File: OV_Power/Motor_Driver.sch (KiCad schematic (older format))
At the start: 15 parts, among them CN1 CONN_HEADER_R_A_2POS_2.5MM, U3 LT6106, U4 VNH5019ATR-E

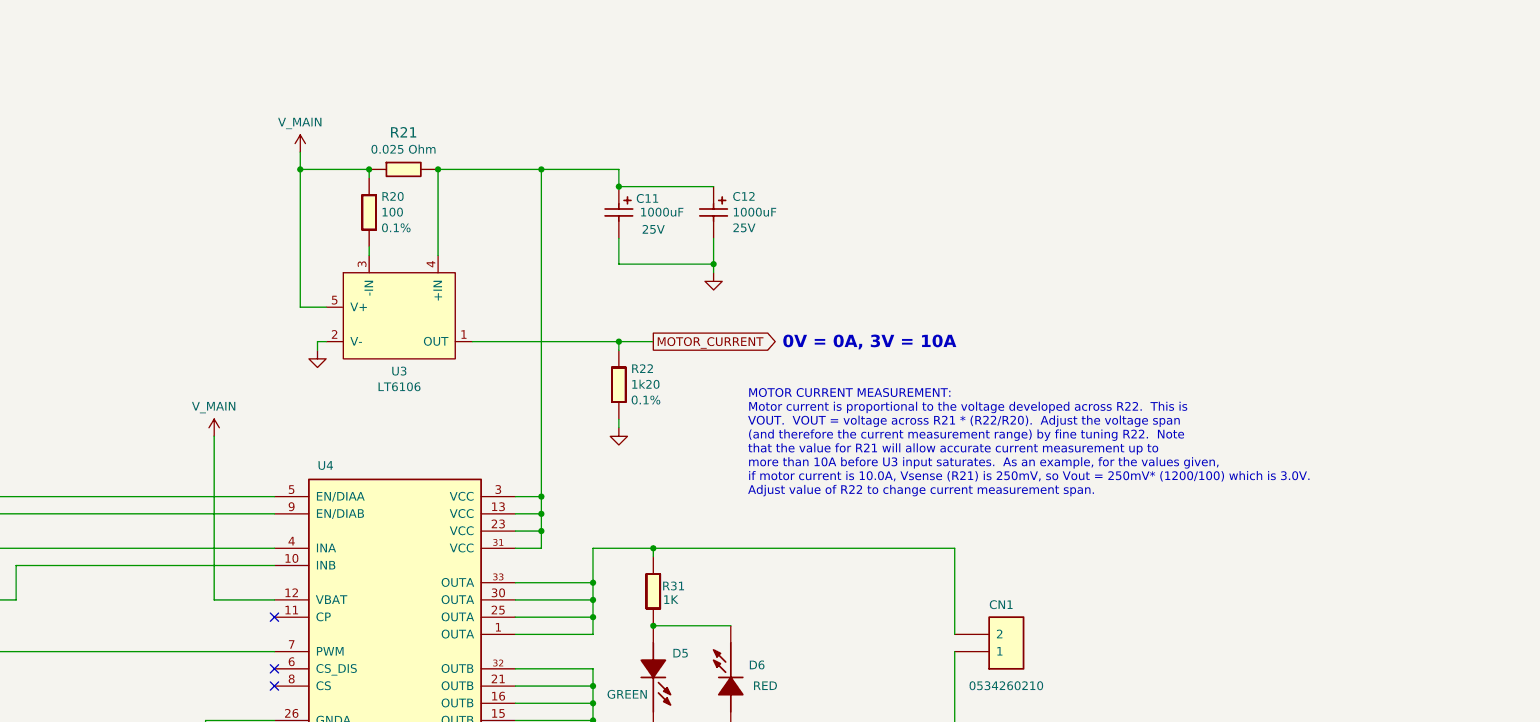
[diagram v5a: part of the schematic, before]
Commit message: First cut at complete routing for the power board.  Still need DRC checking and final fettling of the BOM and silkscreens before going to press.
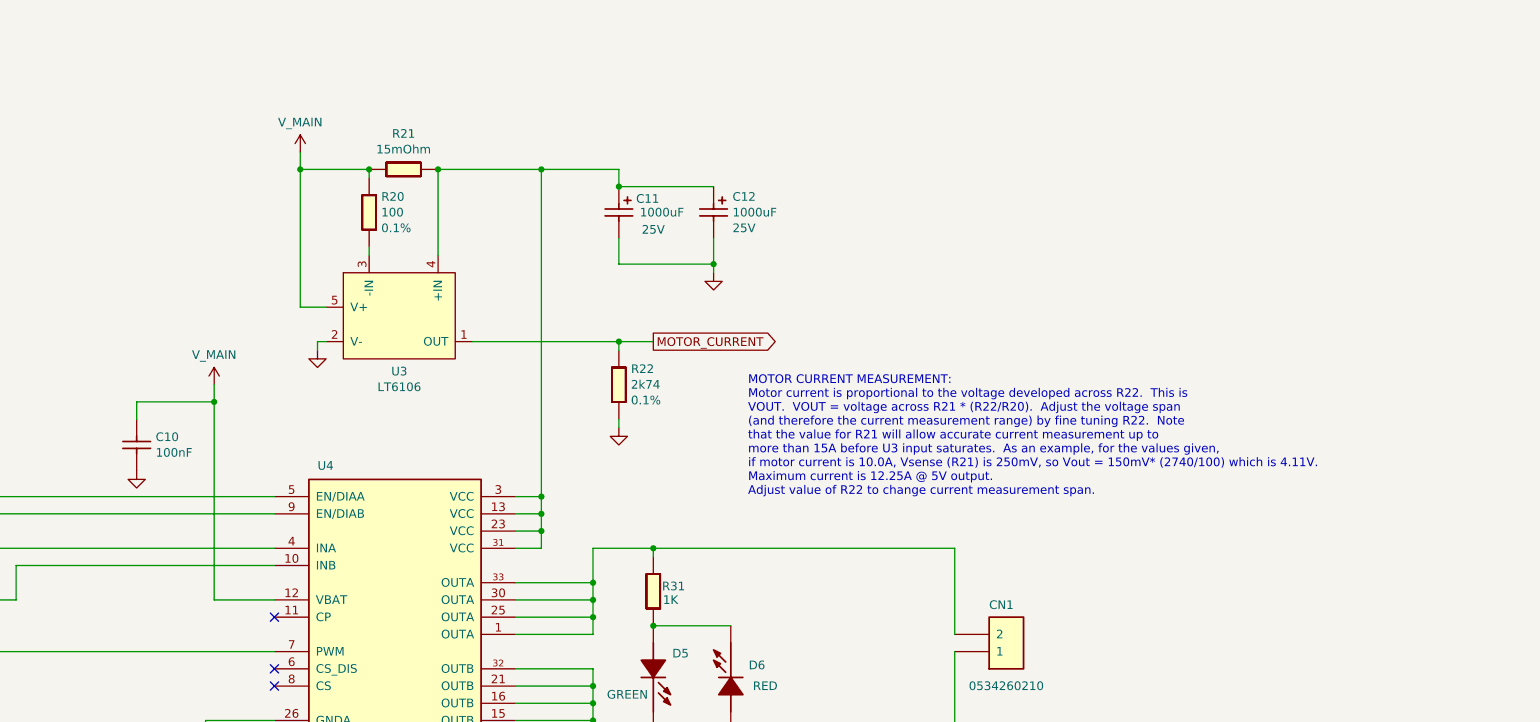
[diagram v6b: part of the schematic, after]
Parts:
- removed R21: 0.025 Ohm, Resistor_SMD:R_2010_5025Metric, symbol OpenVent:Resistor_2010_0.025OHM_sensing_1%_1W
- removed R22: R_0603_1k2_0.1W_0.1%, Resistor_SMD:R_0603_1608Metric, symbol OpenVent:R_0603_1k2_0.1W_0.1%
- added C10: 100nF_0603_Ceramic_Capacitor,_10%,_X7R,_25V, Capacitor_SMD:C_0603_1608Metric, symbol OpenVent:100nF_0603_Ceramic_Capacitor,_10%,_X7R,_25V
- added R21: R_2512_15m_cursense, Resistor_SMD:R_2512_6332Metric, symbol OpenVent:R_2512_15m_cursense
- added R22: R_0603_2k74_0.1W_0.1%, Resistor_SMD:R_0603_1608Metric, symbol OpenVent:R_0603_2k74_0.1W_0.1%
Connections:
- net GND: now also C10.2, R22.2
- net MOTOR_CURRENT: now also R22.1
- net V_MAIN: now also C10.1, R21.1
- net at C11.1 (+), C12.1 (+), U3.4 (+IN)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: now also R21.2
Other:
- note added: "MOTOR CURRENT MEASUREMENT:\nMotor current is proportional to the voltage developed across R22. This is\nVOUT. VOUT = voltage across R21 * (R22/R20). Adjust the voltage span\n(and therefore the current measurement range) by fine tuning R22. Note\nthat the value for R21 will allow accurate current measurement up to\nmore than 15A before U3 input saturates. As an example, for the values given,\nif m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"
- note removed: "0V = 0A, 3V = 10A"
- note removed: "MOTOR CURRENT MEASUREMENT:\nMotor current is proportional to the voltage developed across R22. This is\nVOUT. VOUT = voltage across R21 * (R22/R20). Adjust the voltage span\n(and therefore the current measurement range) by fine tuning R22. Note\nthat the value for R21 will allow accurate current measurement up to\nmore than 10A before U3 input saturates. As an example, for the values given,\nif m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"
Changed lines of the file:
@@
 	4200 3650 4550 3650
 Wire Wire Line
-	4200 2700 4200 3650
+	4200 2400 4200 2500
 Wire Wire Line
 	6400 4500 6400 4350
@@
 L OpenVent:V_MAIN #PWR019
 U 1 1 5FC35966
-P 4200 2700
-F 0 "#PWR019" H 4200 2550 50  0001 C CNN
-F 1 "V_MAIN" H 4200 2873 50  0000 C CNN
-F 2 "" H 4200 2700 50  0001 C CNN
-F 3 "" H 4200 2700 50  0001 C CNN
-	1    4200 2700
+P 4200 2400
+F 0 "#PWR019" H 4200 2250 50  0001 C CNN
+F 1 "V_MAIN" H 4200 2573 50  0000 C CNN
+F 2 "" H 4200 2400 50  0001 C CNN
+F 3 "" H 4200 2400 50  0001 C CNN
+	1    4200 2400
 	1    0    0    -1
 $EndComp
@@
 Connection ~ 6550 2150
 Text Notes 7300 3050 0    50   ~ 0
-MOTOR CURRENT MEASUREMENT:\nMotor current is proportional to the voltage developed across R22.  This is\nVOUT.  VOUT = voltage across R21 * (R22/R20).  Adjust the voltage span\n(and therefore the current measurement range) by fine tuning R22.  Note\nthat the value for R21 will allow accurate current measurement up to\nmore than 10A before U3 input saturates.  As an example, for the values given,\nif motor current is 10.0A, Vsense (R21) is 250mV, so Vout = 250mV* (1200/100) which is 3.0V.\nAdjust value of R22 to change current measurement span.
-$Comp
-L OpenVent:Resistor_2010_0.025OHM_sensing_1%_1W R21
-U 1 1 5FD70E6B
-P 5200 1050
-F 0 "R21" H 5300 1163 60  0000 C CNN
-F 1 "0.025 Ohm" H 5300 1065 50  0000 C CNN
-F 2 "Resistor_SMD:R_2010_5025Metric" H 5200 750 60  0001 C CNN
-F 3 "" H 5200 1050 60  0001 C CNN
-F 4 "Vishay Dale" H 5900 1000 50  0001 C CNN "Manufacturer"
-F 5 "WSL2010R0250FEA18" H 5850 850 50  0001 C CNN "Mfr_PN"
-	1    5200 1050
-	1    0    0    -1
-$EndComp
-$Comp
-L OpenVent:R_0603_1k2_0.1W_0.1% R22
-U 1 1 5FD757C1
+MOTOR CURRENT MEASUREMENT:\nMotor current is proportional to the voltage developed across R22.  This is\nVOUT.  VOUT = voltage across R21 * (R22/R20).  Adjust the voltage span\n(and therefore the current measurement range) by fine tuning R22.  Note\nthat the value for R21 will allow accurate current measurement up to\nmore than 15A before U3 input saturates.  As an example, for the values given,\nif motor current is 10.0A, Vsense (R21) is 250mV, so Vout = 150mV* (2740/100) which is 4.11V.\nMaximum current is 12.25A @ 5V output.\nAdjust value of R22 to change current measurement span.
+Wire Wire Line
+	6550 1250 7100 1250
+Wire Wire Line
+	6100 1150 6550 1150
+Wire Wire Line
+	6550 1150 6550 1250
+Connection ~ 6100 1150
+Connection ~ 6550 1250
+$Comp
+L OpenVent:R_0603_2k74_0.1W_0.1% R22
+U 1 1 5FD3A248
 P 6650 2300
 F 0 "R22" V 6659 2270 50  0000 L CNN
-F 1 "R_0603_1k2_0.1W_0.1%" H 6650 2300 50  0001 C CNN
+F 1 "R_0603_2k74_0.1W_0.1%" H 6650 2300 50  0001 C CNN
 F 2 "Resistor_SMD:R_0603_1608Metric" H 6650 2300 60  0001 C CNN
-F 3 "https://www.yageo.com/upload/media/product/productsearch/datasheet/rchip/PYu-RT_1-to-0.01_RoHS_L_12.pdf" H 6650 2300 50  0001 C CNN
-F 4 "1k20" V 6750 2270 50  0000 L CNN "Val"
+F 3 "https://www.yageo.com/upload/media/product/productsearch/datasheet/rchip/PYu-RT_1-to-0.01_RoHS_L_12.pdf" H 6650 2300 60  0001 C CNN
+F 4 "2k74" V 6750 2270 50  0000 L CNN "Val"
 F 5 "0.1%" V 6841 2270 50  0000 L CNN "Tolerance"
 F 6 "0.1W" H 6650 2300 50  0001 C CNN "Watt"
 F 7 "Yageo" H 6650 2300 50  0001 C CNN "Mfr"
-F 8 "RT0603BRD071K2L" H 6650 2300 50  0001 C CNN "Mfr_PN"
-F 9 "RES SMD 1.2K OHM 0.1% 1/10W 0603" H 6650 2300 50  0001 C CNN "Desc"
-F 10 "1.2 kOhms ±0.1% 0.1W, 1/10W Chip Resistor 0603 (1608 Metric)  Thin Film" H 6650 2300 50  0001 C CNN "Detailed"
+F 8 "RT0603BRE072K74L" H 6650 2300 50  0001 C CNN "Mfr_PN"
+F 9 "RES SMD 2.74KOHM 0.1% 1/10W 0603" H 6650 2300 50  0001 C CNN "Desc"
+F 10 "2.74 kOhms ±0.1% 0.1W, 1/10W Chip Resistor 0603 (1608 Metric)  Thin Film" H 6650 2300 50  0001 C CNN "Detailed"
 	1    6650 2300
 	0    1    1    0
+$EndComp
+$Comp
+L OpenVent:R_2512_15m_cursense R21
+U 1 1 5FD98E9C
+P 5300 1150
+F 0 "R21" H 5300 1357 50  0000 C CNN
+F 1 "R_2512_15m_cursense" H 5530 1110 50  0001 L CNN
+F 2 "Resistor_SMD:R_2512_6332Metric" H 5500 1150 50  0001 C CNN
+F 3 "https://riedon.com/media/pdf/CSR.pdf" H 5500 1150 50  0001 C CNN
+F 4 "15mOhm" H 5300 1266 50  0000 C CNN "Val"
+F 5 "1%" H 5500 1150 50  0001 C CNN "tol"
+F 6 "2W" H 5500 1150 50  0001 C CNN "Watt"
+F 7 "Riedon" H 5500 1150 50  0001 C CNN "Mfr"
+F 8 "CSR2512A0R015F" H 5500 1150 50  0001 C CNN "Mfr_Pn"
+F 9 "RES 0.015 OHM 1% 2W 2512" H 5500 1150 50  0001 C CNN "Desc"
+F 10 "15 mOhms ±1% 2W Chip Resistor 2512 (6432 Metric) Current Sense, Non-Inductive Metal Element" H 5500 1150 50  0001 C CNN "Detailed"
+	1    5300 1150
+	1    0    0    -1
 $EndComp
 Connection ~ 5100 1150
 Connection ~ 5500 1150
-Text Notes 7500 2200 0    71   ~ 14
-0V = 0A, 3V = 10A
-Wire Wire Line
-	6550 1250 7100 1250
-Wire Wire Line
-	6100 1150 6550 1150
-Wire Wire Line
-	6550 1150 6550 1250
-Connection ~ 6100 1150
-Connection ~ 6550 1250
+$Comp
+L OpenVent:100nF_0603_Ceramic_Capacitor,_10%,_X7R,_25V C10
+U 1 1 5FDC2D70
+P 3850 2700
+F 0 "C10" V 3854 2710 50  0000 L CNN
+F 1 "100nF_0603_Ceramic_Capacitor,_10%,_X7R,_25V" H 3850 2700 50  0001 C CNN
+F 2 "Capacitor_SMD:C_0603_1608Metric" H 3850 2700 50  0001 C CNN
+F 3 "" H 3850 2700 50  0001 C CNN
+F 4 "100nF" V 3945 2710 50  0000 L CNN "Val"
+F 5 "25V" H 3850 2700 50  0001 C CNN "Voltage"
+F 6 "10%" H 3850 2700 50  0001 C CNN "Tolerance"
+	1    3850 2700
+	0    1    1    0
+$EndComp
+$Comp
+L OpenVent:GND #GND_0101
+U 1 1 5FDC42B3
+P 3750 2900
+F 0 "#GND_0101" H 3750 2900 20  0001 C CNN
+F 1 "GND" H 3750 2830 50  0001 C CNN
+F 2 "" H 3750 2900 70  0000 C CNN
+F 3 "" H 3750 2900 70  0000 C CNN
+	1    3750 2900
+	1    0    0    -1
+$EndComp
+Wire Wire Line
+	3750 2600 3750 2500
+Wire Wire Line
+	3750 2500 4200 2500
+Connection ~ 4200 2500
+Wire Wire Line
+	4200 2500 4200 3650
 $EndSCHEMATC

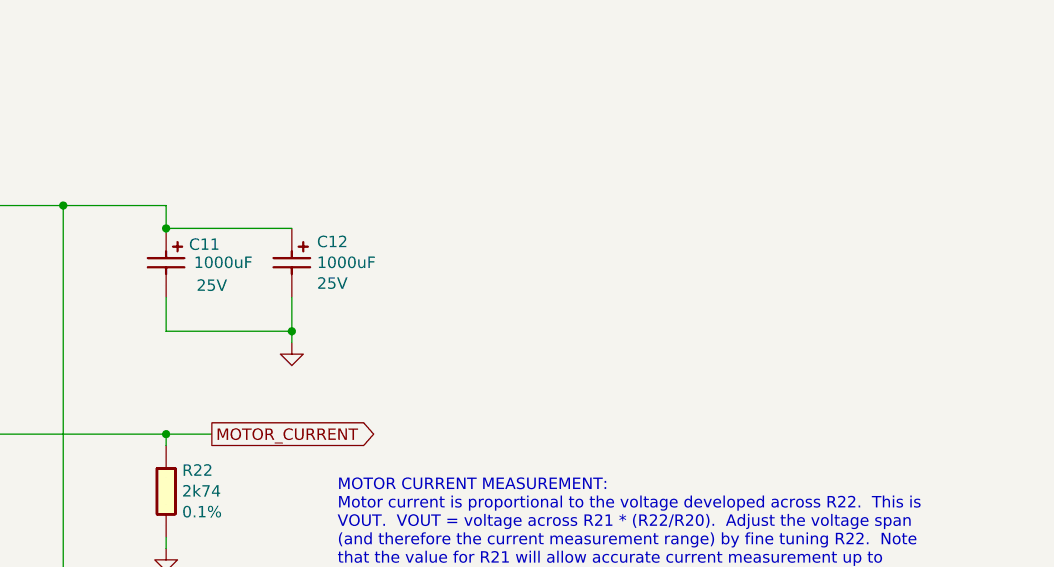
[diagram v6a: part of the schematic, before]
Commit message: Tentative placement (again...) for power board, also added a ferrite part for Shrouk to the main library.
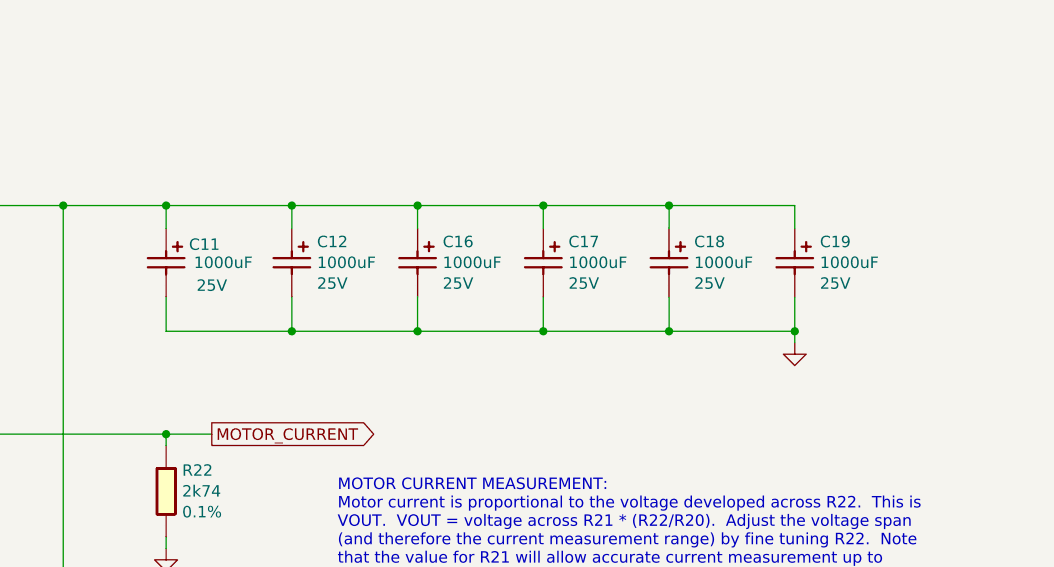
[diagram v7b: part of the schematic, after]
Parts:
- added C16, C17, C18, C19: 1000uF_25V_Aluminium_SMD_Capacitor,_20%, Capacitor_SMD:CP_Elec_10x10, symbol OpenVent:1000uF_25V_Aluminium_SMD_Capacitor,_20%
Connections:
- net GND: now also C16.2 (-), C17.2 (-), C18.2 (-), C19.2 (-)
- net at C11.1 (+), C12.1 (+), R21.2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: now also C16.1 (+), C17.1 (+), C18.1 (+), C19.1 (+)
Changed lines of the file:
@@
 L OpenVent:GND #GND_016
 U 1 1 5F8DD12E
-P 7100 1750
-F 0 "#GND_016" H 7100 1750 20  0001 C CNN
-F 1 "GND" H 7100 1680 50  0001 C CNN
-F 2 "" H 7100 1750 70  0000 C CNN
-F 3 "" H 7100 1750 70  0000 C CNN
-	1    7100 1750
+P 9300 1750
+F 0 "#GND_016" H 9300 1750 20  0001 C CNN
+F 1 "GND" H 9300 1680 50  0001 C CNN
+F 2 "" H 9300 1750 70  0000 C CNN
+F 3 "" H 9300 1750 70  0000 C CNN
+	1    9300 1750
 	1    0    0    -1
 $EndComp
@@
 Wire Wire Line
 	7100 1700 6550 1700
-Wire Wire Line
-	7100 1750 7100 1700
 Wire Wire Line
 	4150 4750 4150 4850
@@
 Connection ~ 6750 4500
 Connection ~ 7200 4500
-Connection ~ 7100 1700
 $Comp
 L OpenVent:1K_0603_Chip_Resistor,_1%,_0.1W R24
@@
 MOTOR CURRENT MEASUREMENT:\nMotor current is proportional to the voltage developed across R22.  This is\nVOUT.  VOUT = voltage across R21 * (R22/R20).  Adjust the voltage span\n(and therefore the current measurement range) by fine tuning R22.  Note\nthat the value for R21 will allow accurate current measurement up to\nmore than 15A before U3 input saturates.  As an example, for the values given,\nif motor current is 10.0A, Vsense (R21) is 250mV, so Vout = 150mV* (2740/100) which is 4.11V.\nMaximum current is 12.25A @ 5V output.\nAdjust value of R22 to change current measurement span.
 Wire Wire Line
-	6550 1250 7100 1250
-Wire Wire Line
 	6100 1150 6550 1150
 Wire Wire Line
 	6550 1150 6550 1250
 Connection ~ 6100 1150
-Connection ~ 6550 1250
 $Comp
 L OpenVent:R_0603_2k74_0.1W_0.1% R22
@@
 Wire Wire Line
 	4200 2500 4200 3650
+$Comp
+L OpenVent:1000uF_25V_Aluminium_SMD_Capacitor,_20% C16
+U 1 1 5FE5727D
+P 7650 1250
+F 0 "C16" V 7709 1360 50  0000 L CNN
+F 1 "1000uF_25V_Aluminium_SMD_Capacitor,_20%" H 7650 1250 50  0001 C CNN
+F 2 "Capacitor_SMD:CP_Elec_10x10" H 7650 1250 60  0001 C CNN
+F 3 "https://www.digikey.com/en/product-highlight/u/united-chemi-con/mzs-series-aluminum-electrolytic-capacitors" H 7650 1250 60  0001 C CNN
+F 4 "1000uF" V 7800 1360 50  0000 L CNN "Val"
+F 5 "25V" V 7891 1360 50  0000 L CNN "Voltage"
+F 6 "CAP ALUM 1000UF 20% 25V SMD" H 7650 1250 50  0001 C CNN "Desc"
+F 7 "Aluminum Electrolytic Capacitors Radial, Can - SMD 60mOhm @ 100kHz 2000 Hrs @ 105°C" H 7650 1250 50  0001 C CNN "Detailed"
+F 8 "DigiKey" H 7650 1250 50  0001 C CNN "DistName"
+F 9 "565-5120-2-ND" H 7650 1250 50  0001 C CNN "Dist_PN"
+F 10 "United Chemi-Con" H 7650 1250 50  0001 C CNN "Mfr"
+F 11 "EMZS250ARA102MJA0G" H 7650 1250 50  0001 C CNN "Mfr_PN"
+F 12 "20%" H 7650 1250 50  0001 C CNN "Tolerance"
+	1    7650 1250
+	0    1    1    0
+$EndComp
+$Comp
+L OpenVent:1000uF_25V_Aluminium_SMD_Capacitor,_20% C17
+U 1 1 5FE579F4
+P 8200 1250
+F 0 "C17" V 8259 1360 50  0000 L CNN
+F 1 "1000uF_25V_Aluminium_SMD_Capacitor,_20%" H 8200 1250 50  0001 C CNN
+F 2 "Capacitor_SMD:CP_Elec_10x10" H 8200 1250 60  0001 C CNN
+F 3 "https://www.digikey.com/en/product-highlight/u/united-chemi-con/mzs-series-aluminum-electrolytic-capacitors" H 8200 1250 60  0001 C CNN
+F 4 "1000uF" V 8350 1360 50  0000 L CNN "Val"
+F 5 "25V" V 8441 1360 50  0000 L CNN "Voltage"
+F 6 "CAP ALUM 1000UF 20% 25V SMD" H 8200 1250 50  0001 C CNN "Desc"
+F 7 "Aluminum Electrolytic Capacitors Radial, Can - SMD 60mOhm @ 100kHz 2000 Hrs @ 105°C" H 8200 1250 50  0001 C CNN "Detailed"
+F 8 "DigiKey" H 8200 1250 50  0001 C CNN "DistName"
+F 9 "565-5120-2-ND" H 8200 1250 50  0001 C CNN "Dist_PN"
+F 10 "United Chemi-Con" H 8200 1250 50  0001 C CNN "Mfr"
+F 11 "EMZS250ARA102MJA0G" H 8200 1250 50  0001 C CNN "Mfr_PN"
+F 12 "20%" H 8200 1250 50  0001 C CNN "Tolerance"
+	1    8200 1250
+	0    1    1    0
+$EndComp
+$Comp
+L OpenVent:1000uF_25V_Aluminium_SMD_Capacitor,_20% C18
+U 1 1 5FE58241
+P 8750 1250
+F 0 "C18" V 8809 1360 50  0000 L CNN
+F 1 "1000uF_25V_Aluminium_SMD_Capacitor,_20%" H 8750 1250 50  0001 C CNN
+F 2 "Capacitor_SMD:CP_Elec_10x10" H 8750 1250 60  0001 C CNN
+F 3 "https://www.digikey.com/en/product-highlight/u/united-chemi-con/mzs-series-aluminum-electrolytic-capacitors" H 8750 1250 60  0001 C CNN
+F 4 "1000uF" V 8900 1360 50  0000 L CNN "Val"
+F 5 "25V" V 8991 1360 50  0000 L CNN "Voltage"
+F 6 "CAP ALUM 1000UF 20% 25V SMD" H 8750 1250 50  0001 C CNN "Desc"
+F 7 "Aluminum Electrolytic Capacitors Radial, Can - SMD 60mOhm @ 100kHz 2000 Hrs @ 105°C" H 8750 1250 50  0001 C CNN "Detailed"
+F 8 "DigiKey" H 8750 1250 50  0001 C CNN "DistName"
+F 9 "565-5120-2-ND" H 8750 1250 50  0001 C CNN "Dist_PN"
+F 10 "United Chemi-Con" H 8750 1250 50  0001 C CNN "Mfr"
+F 11 "EMZS250ARA102MJA0G" H 8750 1250 50  0001 C CNN "Mfr_PN"
+F 12 "20%" H 8750 1250 50  0001 C CNN "Tolerance"
+	1    8750 1250
+	0    1    1    0
+$EndComp
+$Comp
+L OpenVent:1000uF_25V_Aluminium_SMD_Capacitor,_20% C19
+U 1 1 5FE58A16
+P 9300 1250
+F 0 "C19" V 9359 1360 50  0000 L CNN
+F 1 "1000uF_25V_Aluminium_SMD_Capacitor,_20%" H 9300 1250 50  0001 C CNN
+F 2 "Capacitor_SMD:CP_Elec_10x10" H 9300 1250 60  0001 C CNN
+F 3 "https://www.digikey.com/en/product-highlight/u/united-chemi-con/mzs-series-aluminum-electrolytic-capacitors" H 9300 1250 60  0001 C CNN
+F 4 "1000uF" V 9450 1360 50  0000 L CNN "Val"
+F 5 "25V" V 9541 1360 50  0000 L CNN "Voltage"
+F 6 "CAP ALUM 1000UF 20% 25V SMD" H 9300 1250 50  0001 C CNN "Desc"
+F 7 "Aluminum Electrolytic Capacitors Radial, Can - SMD 60mOhm @ 100kHz 2000 Hrs @ 105°C" H 9300 1250 50  0001 C CNN "Detailed"
+F 8 "DigiKey" H 9300 1250 50  0001 C CNN "DistName"
+F 9 "565-5120-2-ND" H 9300 1250 50  0001 C CNN "Dist_PN"
+F 10 "United Chemi-Con" H 9300 1250 50  0001 C CNN "Mfr"
+F 11 "EMZS250ARA102MJA0G" H 9300 1250 50  0001 C CNN "Mfr_PN"
+F 12 "20%" H 9300 1250 50  0001 C CNN "Tolerance"
+	1    9300 1250
+	0    1    1    0
+$EndComp
+Wire Wire Line
+	6550 1150 7100 1150
+Wire Wire Line
+	9300 1150 9300 1250
+Connection ~ 6550 1150
+Wire Wire Line
+	8750 1150 8750 1250
+Connection ~ 8750 1150
+Wire Wire Line
+	8750 1150 9300 1150
+Wire Wire Line
+	8200 1250 8200 1150
+Connection ~ 8200 1150
+Wire Wire Line
+	8200 1150 8750 1150
+Wire Wire Line
+	7650 1250 7650 1150
+Connection ~ 7650 1150
+Wire Wire Line
+	7650 1150 8200 1150
+Wire Wire Line
+	7100 1250 7100 1150
+Connection ~ 7100 1150
+Wire Wire Line
+	7100 1150 7650 1150
+Wire Wire Line
+	7100 1700 7650 1700
+Wire Wire Line
+	9300 1700 9300 1750
+Connection ~ 7100 1700
+Wire Wire Line
+	9300 1550 9300 1700
+Connection ~ 9300 1700
+Wire Wire Line
+	8750 1550 8750 1700
+Connection ~ 8750 1700
+Wire Wire Line
+	8750 1700 9300 1700
+Wire Wire Line
+	8200 1550 8200 1700
+Connection ~ 8200 1700
+Wire Wire Line
+	8200 1700 8750 1700
+Wire Wire Line
+	7650 1550 7650 1700
+Connection ~ 7650 1700
+Wire Wire Line
+	7650 1700 8200 1700
 $EndSCHEMATC
